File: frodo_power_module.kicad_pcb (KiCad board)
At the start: 2 copper layers, 76 parts, among them J1 Keystone 1048, J10 SWD Header, J2 Molex MicroFit 2x3, J3 Molex MicroFit 2x2, J4 Molex MicroFit 2x2, J5 JST-GH, J6 JST-GH, J7 Molex MicroFit 2x3, U1 STM32F042F6Px, U2 L7805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

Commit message: worked on file
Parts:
- moved C3 117.2 mm to (132.5, 91.8)
- moved C1 114.2 mm to (117.5, 99.8), turned to 90 degrees
- moved R20 113.2 mm to (103.8, 98.5), turned to 90 degrees
- moved C2 111.9 mm to (117.5, 94.8), turned to 90 degrees
- moved C5 111.9 mm to (137.0, 80.2)
- moved R21 111.7 mm to (103.8, 94.5), turned to 90 degrees
- moved C4 109.4 mm to (140.5, 95.5), turned to -90 degrees
- moved U3 107.9 mm to (134.6, 96.8), turned to 0 degrees
- moved R22 104.7 mm to (110.5, 95.0), turned to 90 degrees
- moved R23 103.7 mm to (110.5, 91.8), turned to 90 degrees
- moved U1 99.8 mm to (133.2, 72.2), turned to -90 degrees
- moved C6 90.9 mm to (135.0, 78.0)
- moved R1 90.1 mm to (131.8, 88.0), turned to 0 degrees
- moved C13 89.2 mm to (146.8, 64.0)
- moved C14 80.5 mm to (145.2, 70.5), turned to -90 degrees
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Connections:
- net SWCLK renamed S-
- net SWDIO renamed S+
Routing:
- net +3V3: track 0.00 -> 46.2 mm
- net +VSW: track 0.00 -> 45.1 mm
- net S+: track 0.00 -> 43.6 mm
- net S-: track 0.00 -> 43.5 mm
- net +5V: track 0.00 -> 34.7 mm
- net Net-(U5-VC1): track 0.00 -> 7.27 mm
- net GND: track 0.00 -> 6.38 mm
- net Net-(U5-VC1_CB): track 0.00 -> 6.21 mm
- net CAN+: track 82.9 -> 88.6 mm, vias 2 -> 3
- net CAN-: track 83.0 -> 88.6 mm, vias 2 -> 3
- net CAN_RX: track 0.00 -> 5.45 mm
- net CAN_TX: track 0.00 -> 5.39 mm
- net Net-(U5-VDD): track 0.00 -> 4.36 mm
- net Net-(J1-Pin_2): track 0.00 -> 4.20 mm, vias 0 -> 1
- net Net-(U5-VC2): track 0.00 -> 3.77 mm
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
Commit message: saving work status
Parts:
- TH1: moved to F.Cu
- moved U4 138.8 mm to (110.3, 83.5)
- moved D2 124.9 mm to (104.8, 77.2)
- moved D3 124.9 mm to (104.8, 79.8)
- moved C12 120.4 mm to (113.5, 81.1), turned to 90 degrees
- moved R6 114.1 mm to (104.9, 84.7), turned to -90 degrees
- moved R25 111.8 mm to (101.5, 77.3), turned to 0 degrees
- moved R5 110.4 mm to (109.6, 86.5), turned to 0 degrees
- moved R26 109.2 mm to (101.4, 79.8), turned to 0 degrees
- moved R24 108.6 mm to (104.9, 88.0), turned to -90 degrees
- moved R8 102.8 mm to (115.4, 83.5), turned to -90 degrees
- moved R9 102.4 mm to (115.9, 86.8), turned to 0 degrees
- moved R10 102.2 mm to (115.9, 88.4), turned to 0 degrees
- moved C20 101.8 mm to (119.4, 74.3), turned to 0 degrees
- moved R7 101.6 mm to (117.0, 83.5), turned to -90 degrees
- moved Y1 100.9 mm to (131.0, 60.6), turned to 0 degrees
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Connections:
- net S+ renamed SWDIO
- net S- renamed SWCLK
- R18 pad 1: Net-(U7-GND) -> Net-(U7-REF)
- R19 pad 2: Net-(U7-GND) -> Net-(U7-REF)
- U7 pad 1: GND -> Net-(U7-REF)
- U7 pad 2: Net-(U7-GND) -> GND
- U7 pad 3: unconnected-(U7-V+-Pad3) -> +3V3
- U7 pad 4: unconnected-(U7-+-Pad4) -> Net-(J1-Pin_1)
- U7 pad 5: unconnected-(U7---Pad5) -> +BATT
- U7 pad 6: unconnected-(U7-Pad6) -> ISENSE
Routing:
- net CHARGE_ENABLE: track 0.00 -> 124.1 mm
- net NTC: track 0.00 -> 110.9 mm, vias 0 -> 3
- net Net-(J1-Pin_1): track 1.71 -> 59.9 mm, vias 0 -> 16
- net VDC: track 0.00 -> 53.0 mm
- net VSENSE_CHARGE: track 0.00 -> 51.9 mm, vias 0 -> 2
- net VSENSE_BATT: track 0.00 -> 45.2 mm, vias 0 -> 3
- net Net-(R10-Pad2): track 0.00 -> 43.7 mm, vias 0 -> 3
- net STAT1: track 0.00 -> 28.8 mm
- net ISENSE: track 0.00 -> 27.7 mm, vias 0 -> 2
- net STAT2: track 0.00 -> 27.6 mm, vias 0 -> 2
- net Net-(D2-K): track 0.00 -> 26.0 mm
- net +BATT: track 0.00 -> 22.2 mm, vias 0 -> 58
- net GND: track 6.38 -> 23.3 mm
- net Net-(D1-K): track 0.00 -> 15.4 mm
- net Net-(D3-K): track 0.00 -> 15.3 mm
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- added copper zone on B.Cu, net +BATT
- added copper zone on F.Cu, net +BATT
- added copper zone on B.Cu, net Net-(J1-Pin_1)
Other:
- board outline added: 91.1 x 72.6 mm

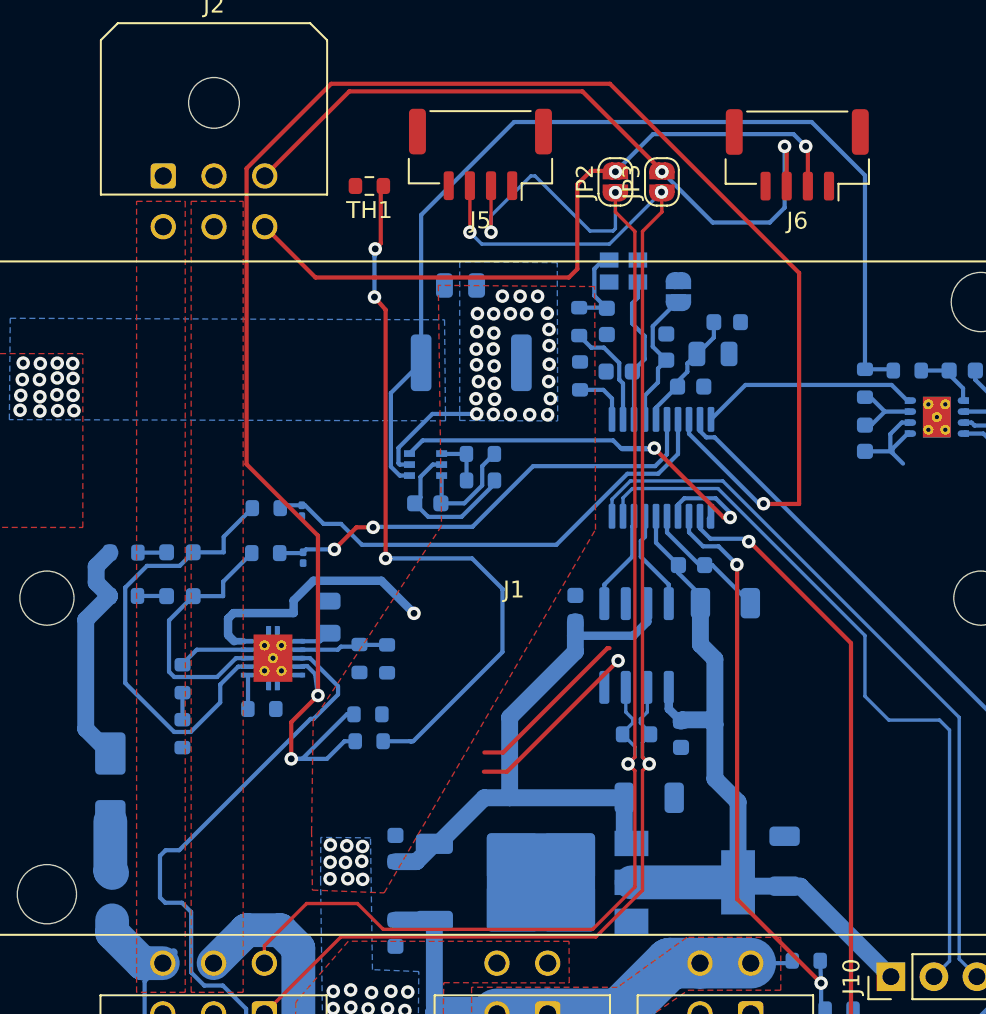
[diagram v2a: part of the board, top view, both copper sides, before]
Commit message: saving work. Almost all routing is done. Ground plane will be added in the next steps to remove all errors and then the goal is to remove all warnings
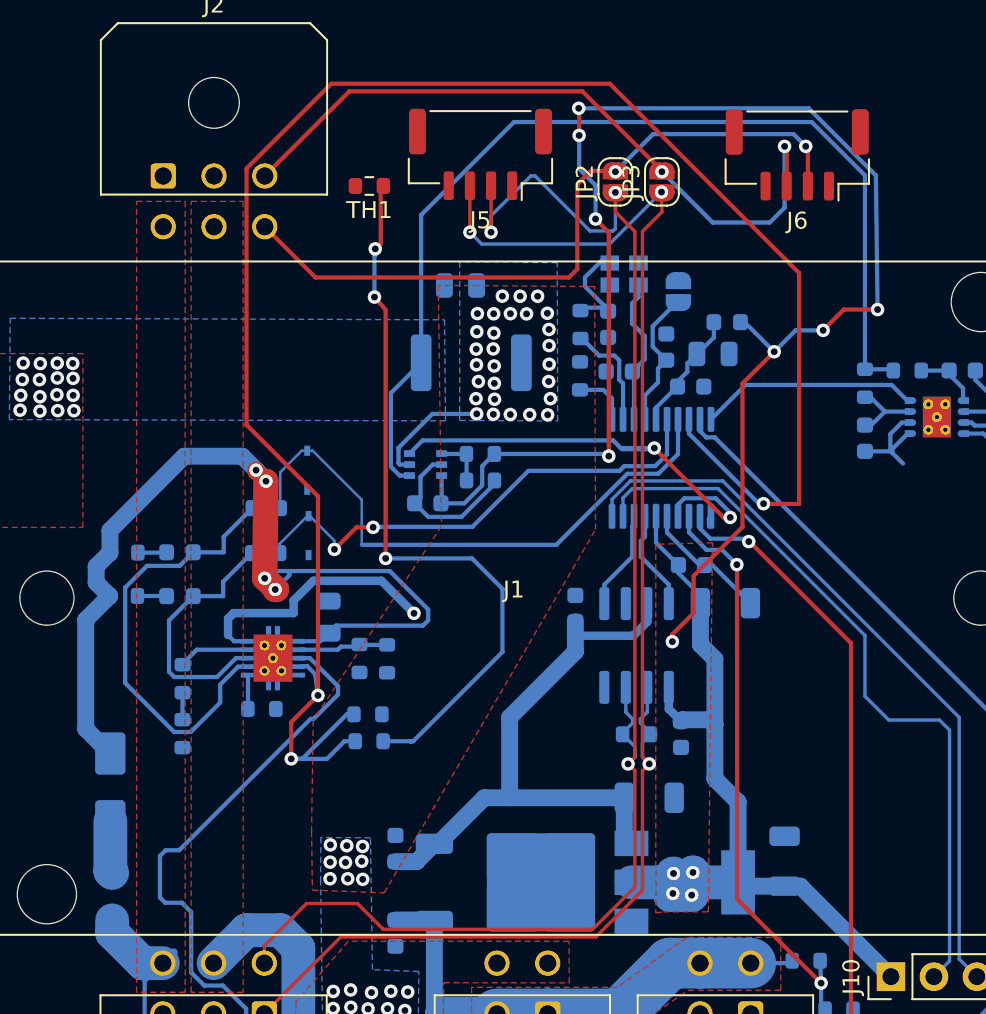
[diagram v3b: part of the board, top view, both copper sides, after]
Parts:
- D5, D6: footprint Diode_SMD:D_0201_0603Metric -> ZenerDiode:SOD323F_DIO
- moved D5 2.41 mm to (112.3, 72.4)
- moved D6 1.34 mm to (112.4, 76.3)
- moved R3 0.19 mm to (128.4, 63.8)
- moved C9 0.19 mm to (130.1, 63.8)
- moved Y1 0.18 mm to (131.0, 60.8)
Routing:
- net +3V3: track 52.4 -> 143.5 mm, vias 0 -> 12
- net Net-(D1-K): track 15.4 -> 55.5 mm, vias 0 -> 4
- net VSENSE_BATT: track 45.2 -> 34.5 mm, vias 3 -> 2
- net VSENSE_CHARGE: track 51.9 -> 41.9 mm
- net STAT1: track 28.8 -> 34.5 mm
- net STAT2: track 27.6 -> 30.2 mm
- added copper zone on F.Cu, net +3V3

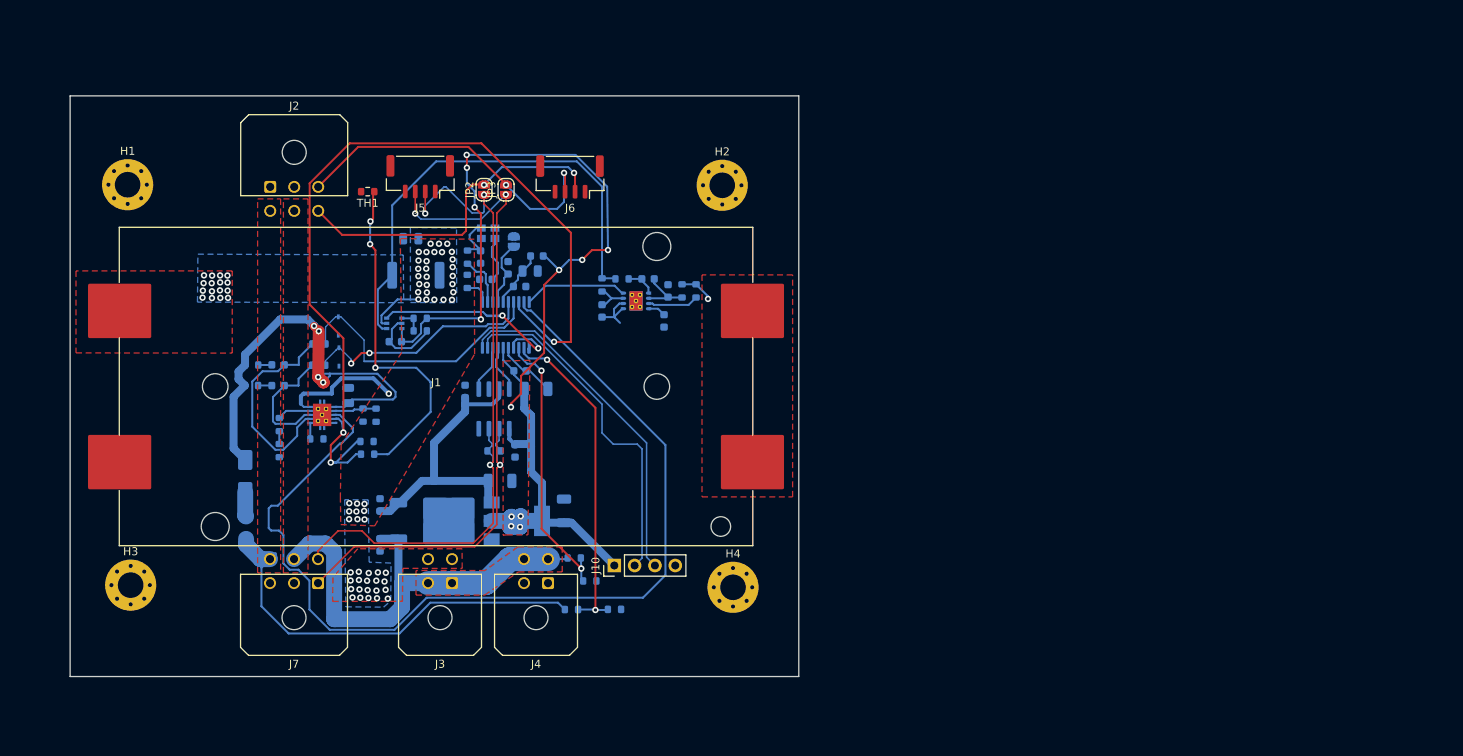
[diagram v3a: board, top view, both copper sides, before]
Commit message: Only warning left to be removed. Also Jumper needs to be implemented and size or width of battery holder needs to be changed
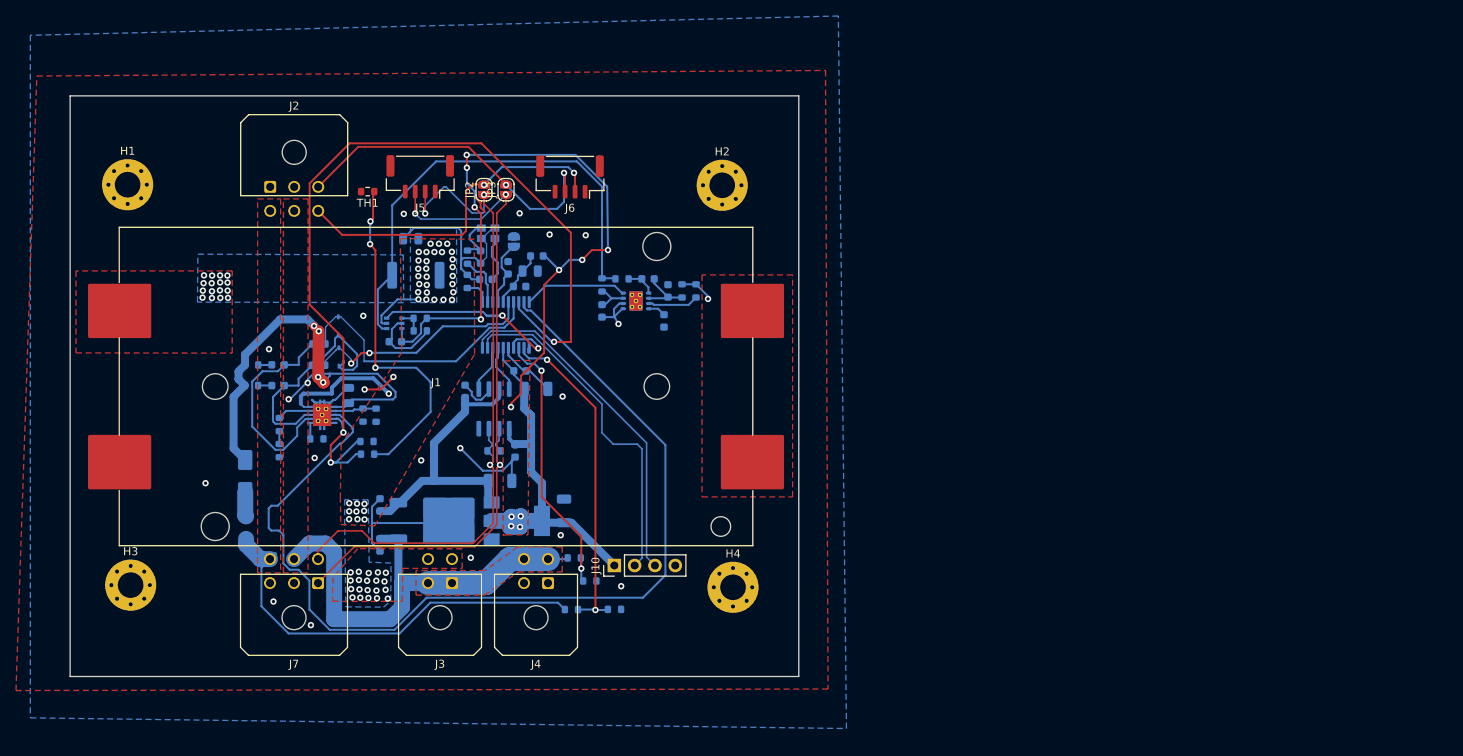
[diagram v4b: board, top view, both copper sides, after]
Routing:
- net GND: track 23.3 -> 118.2 mm, vias 0 -> 21
- net (no net): track 0.00 -> 2.22 mm
- added copper zone on B.Cu, net GND
- added copper zone on F.Cu, net GND

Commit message: modified
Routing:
- net (no net): track 2.22 -> 0.00 mm
- net GND: vias 21 -> 22
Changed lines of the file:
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@@
   (gr_rect (start 78.760362 43.621378) (end 169.844089 116.20039)
     (stroke (width 0.1) (type default)) (fill none) (layer "Edge.Cuts"))
-  (segment (start 130.075 57.008552) (end 130.075 57.585378) (width 0.25) (layer "F.Cu") (net 0))
-  (segment (start 130.075 57.585378) (end 130.611289 58.121667) (width 0.25) (layer "F.Cu") (net 0))
-  (segment (start 129.449277 56.382829) (end 130.075 57.008552) (width 0.25) (layer "F.Cu") (net 0))
   (segment (start 115.571731 80.316261) (end 117.613439 80.316261) (width 0.25) (layer "F.Cu") (net 1))
   (segment (start 117.613439 80.316261) (end 119.175053 78.754647) (width 0.25) (layer "F.Cu") (net 1))
   (segment (start 115.571731 80.316261) (end 115.571731 80.477885) (width 0.25) (layer "F.Cu") (net 1))
   (via (at 128.845581 101.360316) (size 0.8) (drill 0.4) (layers "F.Cu" "B.Cu") (free) (net 1))
+  (via (at 135.192297 71.804074) (size 0.8) (drill 0.4) (layers "F.Cu" "B.Cu") (free) (net 1))
   (via (at 103.628899 75.282457) (size 0.8) (drill 0.4) (layers "F.Cu" "B.Cu") (free) (net 1))
   (via (at 147.643243 104.913766) (size 0.8) (drill 0.4) (layers "F.Cu" "B.Cu") (free) (net 1))
@@
   (zone (net 23) (net_name "Net-(J1-Pin_1)") (layer "F.Cu") (hatch edge 0.5)
     (priority 2)
-    (connect_pads (clearance 0.3))
+    (connect_pads yes (clearance 0.3))
     (min_thickness 0.25) (filled_areas_thickness no)
     (fill yes (thermal_gap 0.5) (thermal_bridge_width 0.5))
@@
   (zone (net 10) (net_name "+BATT") (layer "F.Cu") (hatch edge 0.5)
     (priority 7)
-    (connect_pads (clearance 0.3))
+    (connect_pads yes (clearance 0.3))
     (min_thickness 0.25) (filled_areas_thickness no)
     (fill yes (thermal_gap 0.5) (thermal_bridge_width 0.5))
@@
   (zone (net 24) (net_name "Net-(J1-Pin_2)") (layer "F.Cu") (hatch edge 0.5)
     (priority 1)
-    (connect_pads (clearance 0.3))
+    (connect_pads yes (clearance 0.3))
     (min_thickness 0.25) (filled_areas_thickness no)
     (fill yes (thermal_gap 0.5) (thermal_bridge_width 0.5))
@@
   (zone (net 22) (net_name "VDC") (layer "F.Cu") (hatch edge 0.5)
     (priority 4)
-    (connect_pads (clearance 0.3))
+    (connect_pads yes (clearance 0.3))
     (min_thickness 0.25) (filled_areas_thickness no)
     (fill yes (thermal_gap 0.5) (thermal_bridge_width 0.5))
@@
   )
   (zone (net 1) (net_name "GND") (layer "F.Cu") (hatch edge 0.5)
-    (connect_pads (clearance 0.3))
+    (connect_pads yes (clearance 0.3))
     (min_thickness 0.25) (filled_areas_thickness no)
     (fill yes (thermal_gap 0.5) (thermal_bridge_width 0.5) (island_removal_mode 1) (island_area_min 10))
@@
   (zone (net 2) (net_name "+VSW") (layer "F.Cu") (hatch edge 0.5)
     (priority 1)
-    (connect_pads (clearance 0.3))
+    (connect_pads yes (clearance 0.3))
     (min_thickness 0.25) (filled_areas_thickness no)
     (fill yes (thermal_gap 0.5) (thermal_bridge_width 0.5))
@@
   (zone (net 2) (net_name "+VSW") (layer "F.Cu") (hatch edge 0.5)
     (priority 3)
-    (connect_pads (clearance 0.3))
+    (connect_pads yes (clearance 0.3))
     (min_thickness 0.25) (filled_areas_thickness no)
     (fill yes (thermal_gap 0.5) (thermal_bridge_width 0.5))

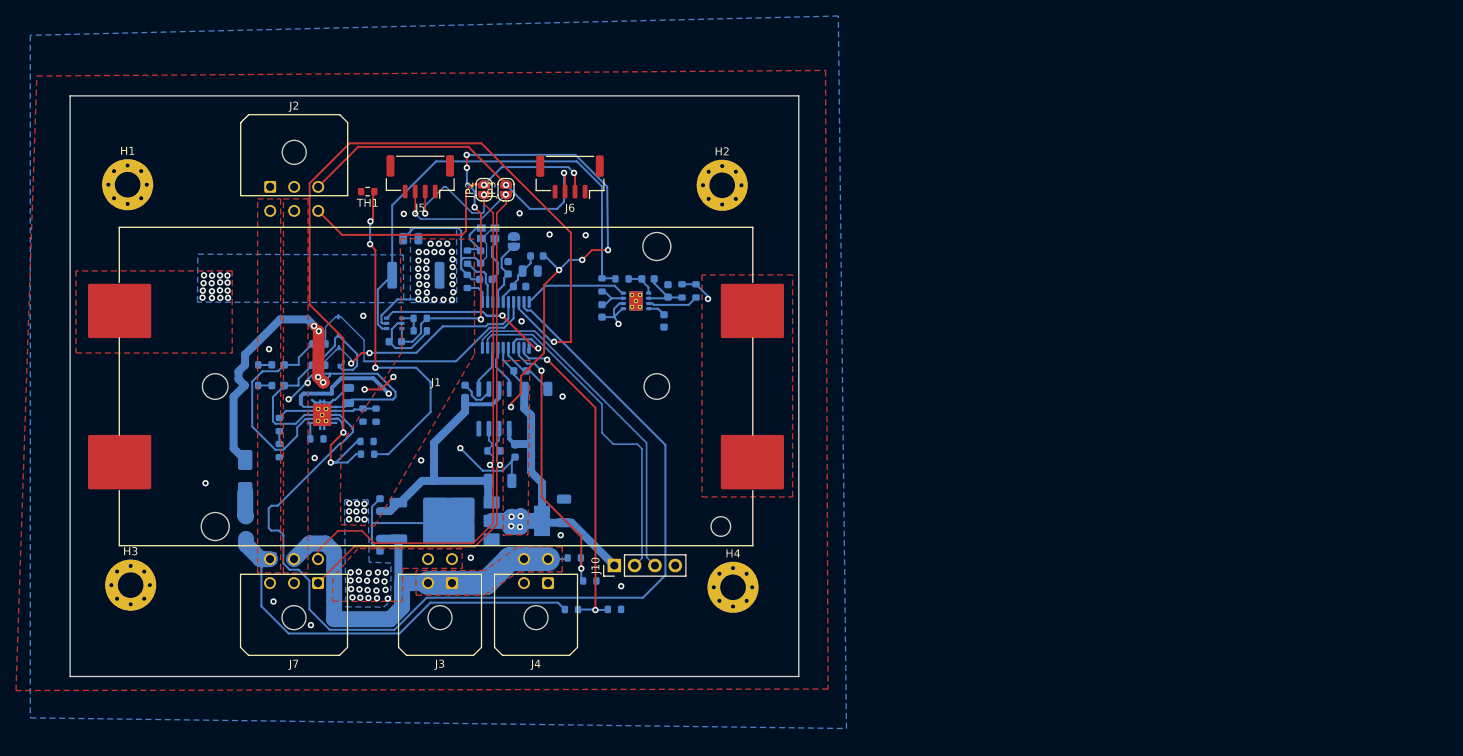
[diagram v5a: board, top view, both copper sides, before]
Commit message: changed PIN layout to suggested one
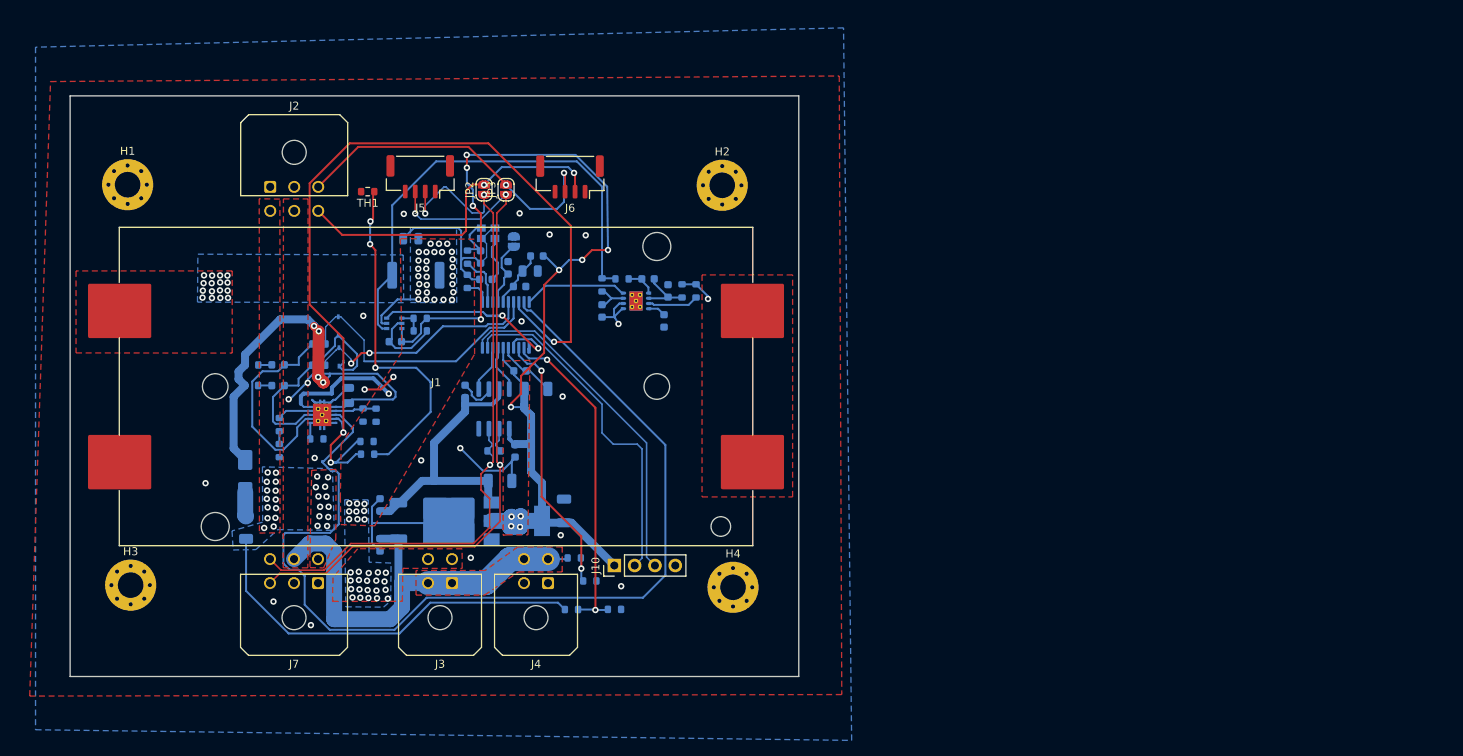
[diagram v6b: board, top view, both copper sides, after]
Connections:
- J7 pad 1: CAN- -> GND
- J7 pad 3: GND -> CAN-
- J7 pad 4: CAN+ -> VDC
- J7 pad 6: VDC -> CAN+
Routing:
- net CAN-: track 88.6 -> 94.6 mm
- net CAN+: track 88.6 -> 94.5 mm
- net CHARGE_ENABLE: track 124.1 -> 126.9 mm
- net VDC: track 53.0 -> 50.5 mm, vias 0 -> 26
- net +3V3: track 143.5 -> 145.6 mm
- net NTC: track 110.9 -> 111.4 mm
- net GND: vias 22 -> 21
- added copper zone on B.Cu, net VDC
